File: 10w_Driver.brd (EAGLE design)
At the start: 47 x 47 mm, 24 parts, among them IC1 78L05Z, T4 2N3904, T5 22-23-2021, T6 22-23-2041, T7 2N3904, T8 2N3904, U1 PT4115PT4115B89E, U2 PT4115PT4115B89E, U3 PT4115PT4115B89E

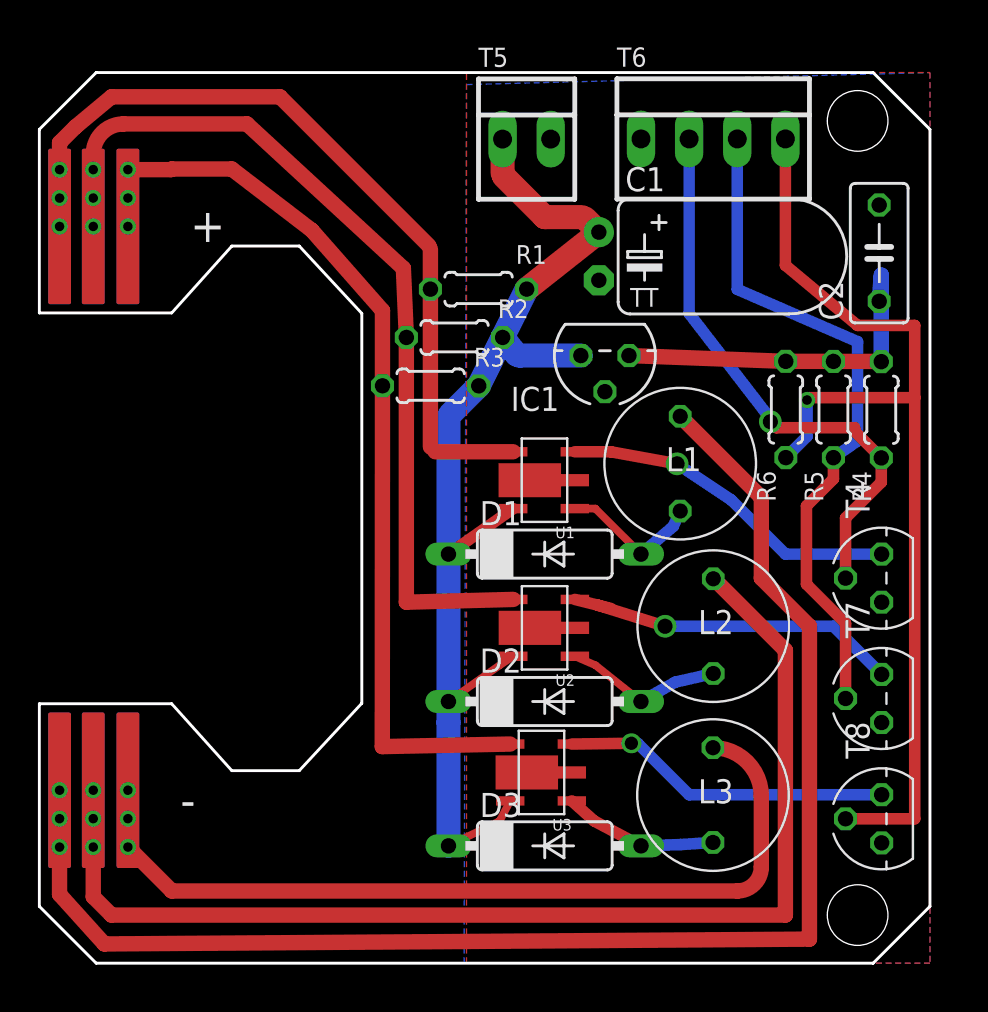
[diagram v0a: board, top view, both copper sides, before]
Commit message: Initial Design with ws2811
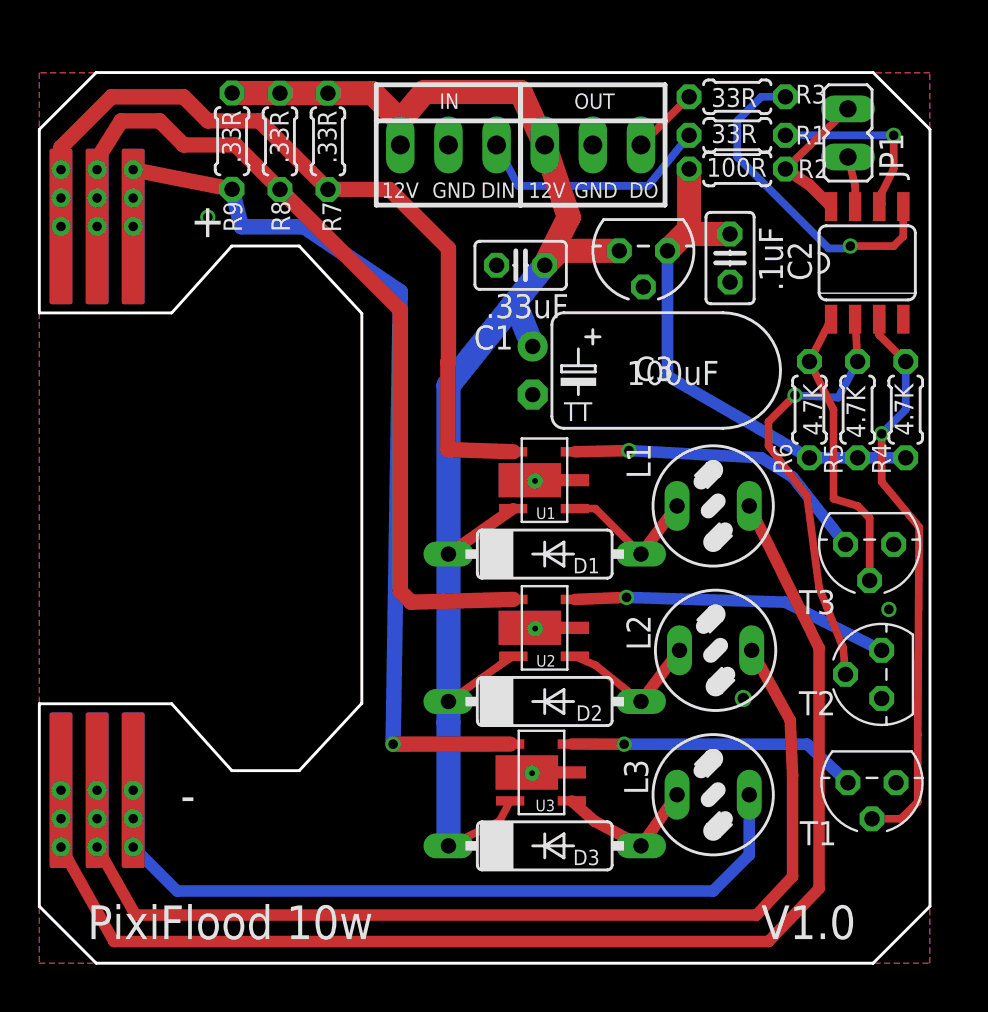
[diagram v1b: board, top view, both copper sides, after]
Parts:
- removed B1: LED-BOARD, MyLibrary:LED-BOARD
- removed T4, T7, T8: 2N3904, transistor:TO92
- removed T5: 22-23-2021, MyLibrary:22-23-2021
- removed T6: 22-23-2041, MyLibrary:22-23-2041
- added C3: 100uF, rcl:TT2D6L
- added IC2: WS2811-SOP8, MyLibrary:SO08-SKINNYPADS
- added JP1: (no value), jumper:JP1
- added R7, R8, R9: .33R, resistor:0204/5
- added T1, T2, T3: 2N3904, transistor:TO92
- added X1, X2: 22-23-2031, MyLibrary:22-23-2031
- added X3, X4, X5, X6, X7, X8: LED-PAD, MyLibrary:LED-PAD
- C1: value EL 100uF -> .33uF; device rcl:TT2D6L -> rcl:C025-025X050
- C2: value MLCC .1uF -> .1uF; device rcl:C050-030X075 -> rcl:C025-025X050
- L1, L2, L3: value 100uH, 6x8mm, 500ma -> 82114R; device MyLibrary:INDUCTOR-6MMX8MM -> inductors:82114R
- R1, R3: value .33Ohm .25w -> 33R; device resistor:0204/5 -> rcl:0204/5
- R2: value .33Ohm .25w -> 100R; device resistor:0204/5 -> rcl:0204/5
- moved R3 22.2 mm to (36.8, 45.7), turned to 0 degrees
- moved R2 17.4 mm to (36.8, 41.9), turned to 0 degrees
- moved R1 15.9 mm to (36.8, 43.7), turned to 0 degrees
- moved C2 7.88 mm to (36.4, 37.2), turned to 270 degrees
- moved IC1 5.89 mm to (31.9, 37.6)
- moved C1 4.15 mm to (25.4, 36.8), turned to 180 degrees
- moved L1 2.83 mm to (35.6, 24.1), turned to 90 degrees
- moved R4 1.29 mm to (45.7, 29.2)
- moved L2 1.28 mm to (35.7, 16.5), turned to 90 degrees
- moved R5 1.27 mm to (43.2, 29.2)
- moved R6 1.25 mm to (40.6, 29.2)
- turned L3 to 90 degrees
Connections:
- new net N$16: IC2.7, JP1.2
- new net N$18: IC2.2, R5.2, T2.2
- new net N$20: IC2.1, R6.2, T3.2
- new net N$7: IC2.5, R3.2
- new net N$8: IC2.6, R1.2
- new net N$9: L2.2, X6.P$1@1, X6.P$1@2, X6.P$1@3
- net +12V: now also C1.1, C3.+, R7.1, R8.1, R9.1, X1.1, X2.1; no longer C1.+, R1.1, R2.1, R3.1, T5.1
- net +5V: now also R2.1, R4.1, R5.1, R6.1; no longer R4.2, R5.2, R6.2
- net BLUE: now also T1.1; no longer T8.1
- net BOUT: now also R9.2, X7.P$1@1, X7.P$1@2, X7.P$1@3; no longer B1.P$5@1, B1.P$5@2, B1.P$5@3, R3.2
- net GND: now also C1.2, C3.-, IC2.4, T1.3, T2.3, T3.3, U1.2A@1, U1.2A@2, U2.2A@1, U2.2A@2, U3.2A@1, U3.2A@2, X1.2, X2.2; no longer C1.-, T4.3, T5.2, T6.1, T7.3, T8.3
- net GOUT: now also R8.2, X5.P$1@1, X5.P$1@2, X5.P$1@3; no longer B1.P$3@1, B1.P$3@2, B1.P$3@3, R2.2
- net GREEN: now also T2.1; no longer T7.1
- net N$1: now also L1.1; no longer L1.P$2
- net N$10: now also L3.2, X8.P$1@1, X8.P$1@2, X8.P$1@3; no longer R4.1, T4.2, T6.2
- net N$14: now also IC2.8, JP1.1, R2.2; no longer R5.1, T6.3, T7.2
- net N$15: now also IC2.3, R4.2, T1.2; no longer R6.1, T6.4, T8.2
- net N$2: now also L3.1; no longer L3.P$2
- net N$3: now also L1.2, X4.P$1@1, X4.P$1@2, X4.P$1@3; no longer B1.P$2@1, B1.P$2@2, B1.P$2@3, L1.P$1
- net N$4: now also R3.1, X2.3; no longer B1.P$4@1, B1.P$4@2, B1.P$4@3, L2.P$1
- net N$5: now also L2.1; no longer L2.P$2
- net N$6: now also R1.1, X1.3; no longer B1.P$6@1, B1.P$6@2, B1.P$6@3, L3.P$1
- net RED: now also T3.1; no longer T4.1
- net ROUT: now also R7.2, X3.P$1@1, X3.P$1@2, X3.P$1@3; no longer B1.P$1@1, B1.P$1@2, B1.P$1@3, R1.2
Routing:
- net N$4: track 61.9 -> 3.59 mm
- net N$9: track 0.00 -> 55.1 mm
- net N$6: track 45.3 -> 12.7 mm
- net N$14: track 35.8 -> 7.72 mm
- net N$15: track 53.6 -> 30.1 mm
- net N$18: track 0.00 -> 23.0 mm, vias 0 -> 1
- net +12V: track 60.8 -> 79.5 mm
- net N$7: track 0.00 -> 17.6 mm, vias 0 -> 1
- net N$20: track 0.00 -> 15.6 mm
- net N$8: track 0.00 -> 9.68 mm, vias 0 -> 1
- net +5V: track 19.3 -> 27.4 mm
- net N$10: track 30.3 -> 37.4 mm, vias 1 -> 0
- net N$3: track 73.6 -> 68.2 mm
- net N$16: track 0.00 -> 2.66 mm
- net BLUE: track 17.5 -> 15.4 mm
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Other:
- board text added: "+"
- board text added: "-"
- board text added: "12V"
- board text added: "DIN"
- board text added: "DO"
- board text added: "GND"
- board text added: "IN"
- board text added: "OUT"
- board text added: "PixiFlood 10w"
- board text added: "V1.0"

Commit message: Final 1.1
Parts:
- R2: value 100R -> 100ohm
- R4, R5, R6: value 4.7K -> 4.7k
- R7, R8, R9: value .33R -> .33
- moved R4 16.5 mm to (45.7, 12.7), turned to 270 degrees
- moved R5 8.98 mm to (44.5, 20.3), turned to 270 degrees
- moved T2 5.12 mm to (40.0, 17.8), turned to 270 degrees
- moved T3 5.11 mm to (39.6, 25.0), turned to 270 degrees
- moved R6 4.39 mm to (44.7, 27.6), turned to 270 degrees
- moved T1 2.74 mm to (41.3, 10.2), turned to 270 degrees
- moved L2 1.66 mm to (34.3, 17.4)
- moved L3 1.49 mm to (34.2, 9.40)
- moved L1 1.42 mm to (34.3, 24.8)
- turned C2 to 90 degrees
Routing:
- net +5V: track 27.4 -> 37.0 mm, vias 0 -> 1
- net GREEN: track 16.8 -> 12.9 mm
- net N$18: track 23.0 -> 19.2 mm
- net RED: track 16.3 -> 12.7 mm
- net N$20: track 15.6 -> 12.1 mm
- net N$15: track 30.1 -> 28.5 mm
- net BLUE: track 15.4 -> 14.1 mm
- net N$3: track 68.2 -> 67.3 mm
- net N$10: track 37.4 -> 36.7 mm
- net N$9: track 55.1 -> 54.5 mm
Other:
- board text added: "V1.1"
- board text removed: "V1.0"

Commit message: Final 1.1 with Inverter
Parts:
- removed C3: 100uF, rcl:TT2D6L
- removed R7, R8, R9: .33, resistor:0204/5
- removed T1, T2, T3: 2N3904, transistor:TO92
- added IC3: TC7W04FTC7W04F, MyLibrary:SO08
- added TP1: TPB2,54, testpad:B2,54
- added TP2: PTR1TP20SQ, testpad:TP20SQ
- C1: value .33uF -> EL 100uF; device rcl:C025-025X050 -> rcl:TT2D6L
- C2: device rcl:C025-025X050 -> resistor:B45181A
- JP1: device jumper:JP1 -> jumper:JP2
- L1, L2, L3: value 82114R -> SLF7045; device inductors:82114R -> inductors:SLF7045
- R1: value 33R -> .3ohm .25w; device rcl:0204/5 -> resistor:R0805
- R2: value 100ohm -> 33R; device rcl:0204/5 -> rcl:M0805
- R3: device rcl:0204/5 -> rcl:M0805
- R4: value 4.7k -> 100ohm; device resistor:0204/5 -> rcl:M0805
- R5: value 4.7k -> .3hm .25w; device resistor:0204/5 -> resistor:M0805
- R6: value 4.7k -> .3ohm .25w; device resistor:0204/5 -> resistor:R0805
- U1, U2, U3: device MyLibrary:SOT89-5 -> IC:SOT89-5
- X2: value 22-23-2031 -> LED-PAD; device MyLibrary:22-23-2031 -> MyLibrary:LED-PAD
- X4: value LED-PAD -> 22-23-2031; device MyLibrary:LED-PAD -> MyLibrary:22-23-2031
- moved X4 47.3 mm to (33.0, 42.5), turned to 0 degrees
- moved R5 40.0 mm to (12.8, 44.9), turned to 90 degrees
- moved R6 38.7 mm to (10.1, 44.9), turned to 90 degrees
- moved X3 32.8 mm to (1.14, 7.62), turned to 180 degrees
- moved X2 28.2 mm to (1.14, 40.4)
- moved R1 21.5 mm to (15.4, 44.9), turned to 90 degrees
- moved R4 21.1 mm to (34.3, 30.5), turned to 180 degrees
- moved JP1 19.4 mm to (27.1, 32.4), turned to 90 degrees
- moved C1 18.3 mm to (43.7, 35.9)
- moved IC1 12.2 mm to (43.8, 39.9), turned to 270 degrees
- moved R2 9.86 mm to (27.7, 38.2)
- moved IC2 9.77 mm to (34.3, 34.3), turned to 90 degrees
- moved R3 7.65 mm to (35.3, 38.2), turned to 180 degrees
- moved C2 3.74 mm to (39.5, 39.4)
- moved X1 2.62 mm to (24.1, 42.5)
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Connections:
- removed net N$20: IC2.1, R6.2, T3.2
- new net N$19: IC2.2, IC3.6
- net +12V: now also C1.+, R1.2, R5.2, R6.2, X4.1; no longer C1.1, C3.+, R7.1, R8.1, R9.1, X2.1
- net +5V: now also C2.+, IC3.8, TP1.TP; no longer C2.1, R2.1, R5.1, R6.1
- net BLUE: now also IC3.7; no longer T1.1
- net BOUT: now also R6.1; no longer R9.2
- net GND: now also C1.-, C2.-, IC3.4, TP2.TP, X4.2; no longer C1.2, C2.2, C3.-, T1.3, T2.3, T3.3, U1.2A@1, U1.2A@2, U2.2A@1, U2.2A@2, U3.2A@1, U3.2A@2, X2.2
- net GOUT: now also R5.1; no longer R8.2
- net GREEN: now also IC3.2; no longer T2.1
- net N$14: now also JP1.2, R4.2; no longer JP1.1, R2.2
- net N$15: now also IC2.1, IC3.3; no longer IC2.3, R4.2, T1.2
- net N$16: now also IC2.3, IC3.1; no longer IC2.7, JP1.2
- net N$18: now also IC2.7, JP1.3; no longer IC2.2, R5.2, T2.2
- net N$3: now also X3.P$1@1, X3.P$1@2, X3.P$1@3; no longer X4.P$1@1, X4.P$1@2, X4.P$1@3
- net N$4: now also X4.3; no longer X2.3
- net N$6: now also R2.1; no longer R1.1
- net N$8: now also R2.2; no longer R1.2
- net RED: now also IC3.5; no longer T3.1
- net ROUT: now also R1.1, X2.P$1@1, X2.P$1@2, X2.P$1@3; no longer R7.2, X3.P$1@1, X3.P$1@2, X3.P$1@3
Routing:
- net N$19: track 0.00 -> 31.8 mm, vias 0 -> 2
- net +12V: track 79.3 -> 96.5 mm
- net N$16: track 2.66 -> 19.1 mm
- net N$15: track 28.5 -> 14.1 mm, vias 1 -> 0
- net N$18: track 19.2 -> 5.05 mm, vias 1 -> 0
- net +5V: track 37.0 -> 51.0 mm
- net N$7: track 17.6 -> 3.88 mm, vias 1 -> 0
- net N$20: track 12.1 -> 0.00 mm
- net BLUE: track 14.1 -> 23.7 mm, vias 1 -> 2
- net GREEN: track 12.9 -> 21.3 mm, vias 1 -> 2
- net N$6: track 12.7 -> 4.46 mm
- net RED: track 12.7 -> 19.2 mm, vias 1 -> 2
- net N$10: track 36.7 -> 42.6 mm
- net BOUT: track 49.9 -> 55.1 mm, vias 1 -> 2
- net N$8: track 9.68 -> 4.95 mm, vias 1 -> 0
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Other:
- board text added: "10W PixiFlood"
- board text added: "AJ Reynolds"
- board text added: "BLU"
- board text added: "GRN"
- board text added: "RED"
- board text added: "v1.1"
- board text removed: "PixiFlood 10w"
- board text removed: "V1.1"

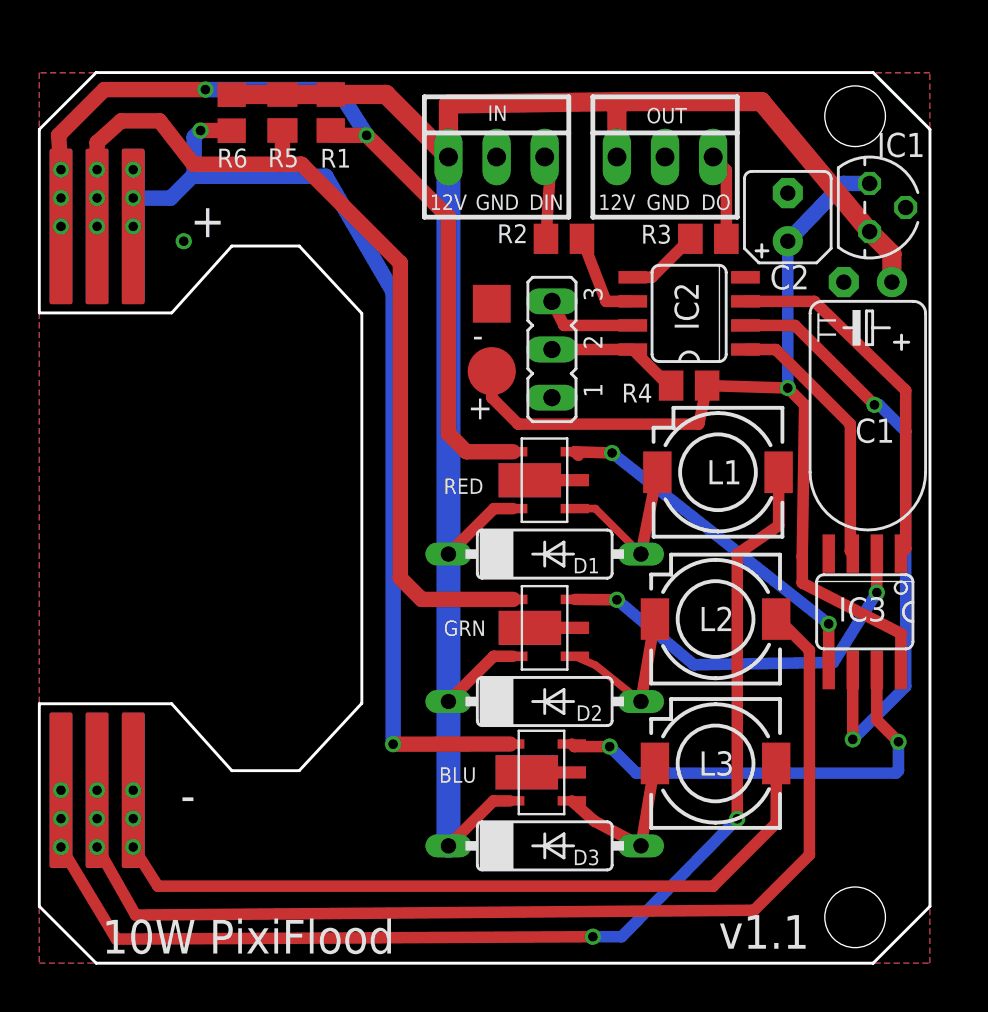
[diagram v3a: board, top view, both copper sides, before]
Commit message: Reworked Inverter Layout
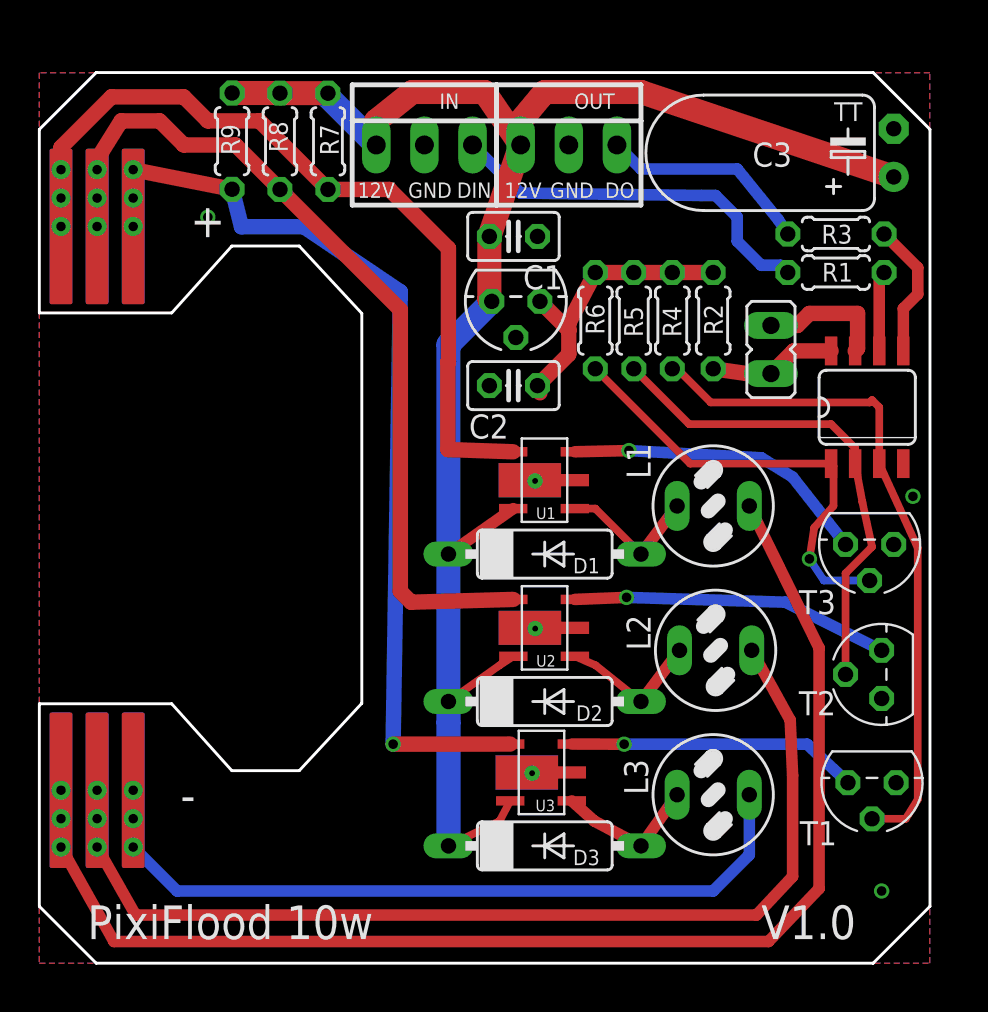
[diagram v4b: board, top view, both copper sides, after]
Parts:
- removed IC3: TC7W04FTC7W04F, MyLibrary:SO08
- removed TP1: TPB2,54, testpad:B2,54
- removed TP2: PTR1TP20SQ, testpad:TP20SQ
- added C3: EL 100uF, rcl:TT2D6L
- added R7, R8, R9: .33Ohm .25w, resistor:0204/5
- added T1, T2, T3: 2N3904, transistor:TO92
- C1: value EL 100uF -> .33uF; device rcl:TT2D6L -> rcl:C025-025X050
- C2: device resistor:B45181A -> rcl:C025-025X050
- JP1: device jumper:JP2 -> jumper:JP1
- L1, L2, L3: value SLF7045 -> 82114R; device inductors:SLF7045 -> inductors:82114R
- R1: value .3ohm .25w -> 33R; device resistor:R0805 -> rcl:0204/5
- R2: value 33R -> 100ohm; device rcl:M0805 -> rcl:0204/5
- R3: device rcl:M0805 -> rcl:0204/5
- R4: value 100ohm -> (none); device rcl:M0805 -> resistor:0204/5
- R5: value .3hm .25w -> (none); device resistor:M0805 -> resistor:0204/5
- R6: value .3ohm .25w -> (none); device resistor:R0805 -> resistor:0204/5
- U1, U2, U3: device IC:SOT89-5 -> MyLibrary:SOT89-5
- X2: value LED-PAD -> 22-23-2031; device MyLibrary:LED-PAD -> MyLibrary:22-23-2031
- X4: value 22-23-2031 -> LED-PAD; device MyLibrary:22-23-2031 -> MyLibrary:LED-PAD
- moved X4 47.3 mm to (1.14, 7.62), turned to 180 degrees
- moved X3 32.8 mm to (1.14, 40.4), turned to 0 degrees
- moved R1 28.0 mm to (42.0, 36.4), turned to 0 degrees
- moved X2 26.9 mm to (27.9, 43.2)
- moved R6 22.1 mm to (29.3, 33.9), turned to 270 degrees
- moved R5 21.5 mm to (31.4, 33.9), turned to 270 degrees
- moved IC1 19.3 mm to (25.1, 34.9), turned to 180 degrees
- moved C1 18.9 mm to (25.0, 38.4), turned to 0 degrees
- moved C2 17.0 mm to (25.0, 30.5), turned to 180 degrees
- moved JP1 11.6 mm to (38.6, 32.4), turned to 0 degrees
- moved IC2 10.6 mm to (43.7, 29.3), turned to 0 degrees
- moved R2 8.98 mm to (35.6, 33.9), turned to 270 degrees
- moved R3 6.74 mm to (42.0, 38.5), turned to 0 degrees
- moved X1 3.86 mm to (20.3, 43.2)
- moved R4 3.54 mm to (33.4, 33.9), turned to 270 degrees
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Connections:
- removed net N$19: IC2.2, IC3.6
- new net N$20: IC2.1, R6.2, T3.2
- net +12V: now also C1.1, C3.+, R7.1, R8.1, R9.1, X2.1; no longer C1.+, R1.2, R5.2, R6.2, X4.1
- net +5V: now also C2.1, R2.1, R5.1, R6.1; no longer C2.+, IC3.8, TP1.TP
- net BLUE: now also T1.1; no longer IC3.7
- net BOUT: now also R9.2; no longer R6.1
- net GND: now also C1.2, C2.2, C3.-, T1.3, T2.3, T3.3, U1.2A@1, U1.2A@2, U2.2A@1, U2.2A@2, U3.2A@1, U3.2A@2, X2.2; no longer C1.-, C2.-, IC3.4, TP2.TP, X4.2
- net GOUT: now also R8.2; no longer R5.1
- net GREEN: now also T2.1; no longer IC3.2
- net N$14: now also JP1.1, R2.2; no longer JP1.2, R4.2
- net N$15: now also IC2.3, R4.2, T1.2; no longer IC2.1, IC3.3
- net N$16: now also IC2.7, JP1.2; no longer IC2.3, IC3.1
- net N$18: now also IC2.2, R5.2, T2.2; no longer IC2.7, JP1.3
- net N$3: now also X4.P$1@1, X4.P$1@2, X4.P$1@3; no longer X3.P$1@1, X3.P$1@2, X3.P$1@3
- net N$4: now also X2.3; no longer X4.3
- net N$6: now also R1.1; no longer R2.1
- net N$8: now also R1.2; no longer R2.2
- net RED: now also T3.1; no longer IC3.5
- net ROUT: now also R7.2, X3.P$1@1, X3.P$1@2, X3.P$1@3; no longer R1.1, X2.P$1@1, X2.P$1@2, X2.P$1@3
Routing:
- net +5V: track 51.0 -> 15.8 mm, vias 1 -> 0
- net N$19: track 31.8 -> 0.00 mm, vias 2 -> 0
- net N$20: track 0.00 -> 23.8 mm, vias 0 -> 1
- net N$15: track 14.1 -> 36.0 mm
- net N$18: track 5.05 -> 26.0 mm
- net N$6: track 4.46 -> 20.1 mm
- net N$16: track 19.1 -> 6.87 mm
- net BLUE: track 23.7 -> 15.4 mm, vias 2 -> 1
- net N$4: track 4.61 -> 11.2 mm
- net BOUT: track 55.1 -> 49.9 mm, vias 2 -> 1
- net N$10: track 42.6 -> 37.4 mm
- net N$3: track 63.5 -> 68.2 mm, vias 2 -> 0
- net GREEN: track 21.3 -> 16.8 mm, vias 2 -> 1
- net ROUT: track 46.8 -> 43.1 mm, vias 2 -> 0
- net +12V: track 96.5 -> 93.0 mm
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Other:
- board text added: "PixiFlood 10w"
- board text added: "V1.0"
- board text removed: "10W PixiFlood"
- board text removed: "AJ Reynolds"
- board text removed: "BLU"
- board text removed: "GRN"
- board text removed: "RED"
- board text removed: "v1.1"
